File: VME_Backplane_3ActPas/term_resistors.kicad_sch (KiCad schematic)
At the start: 32 parts, among them X2H1 HI_L, X2L1 LO_L, X3H1 HI_R, X3L1 LO_R

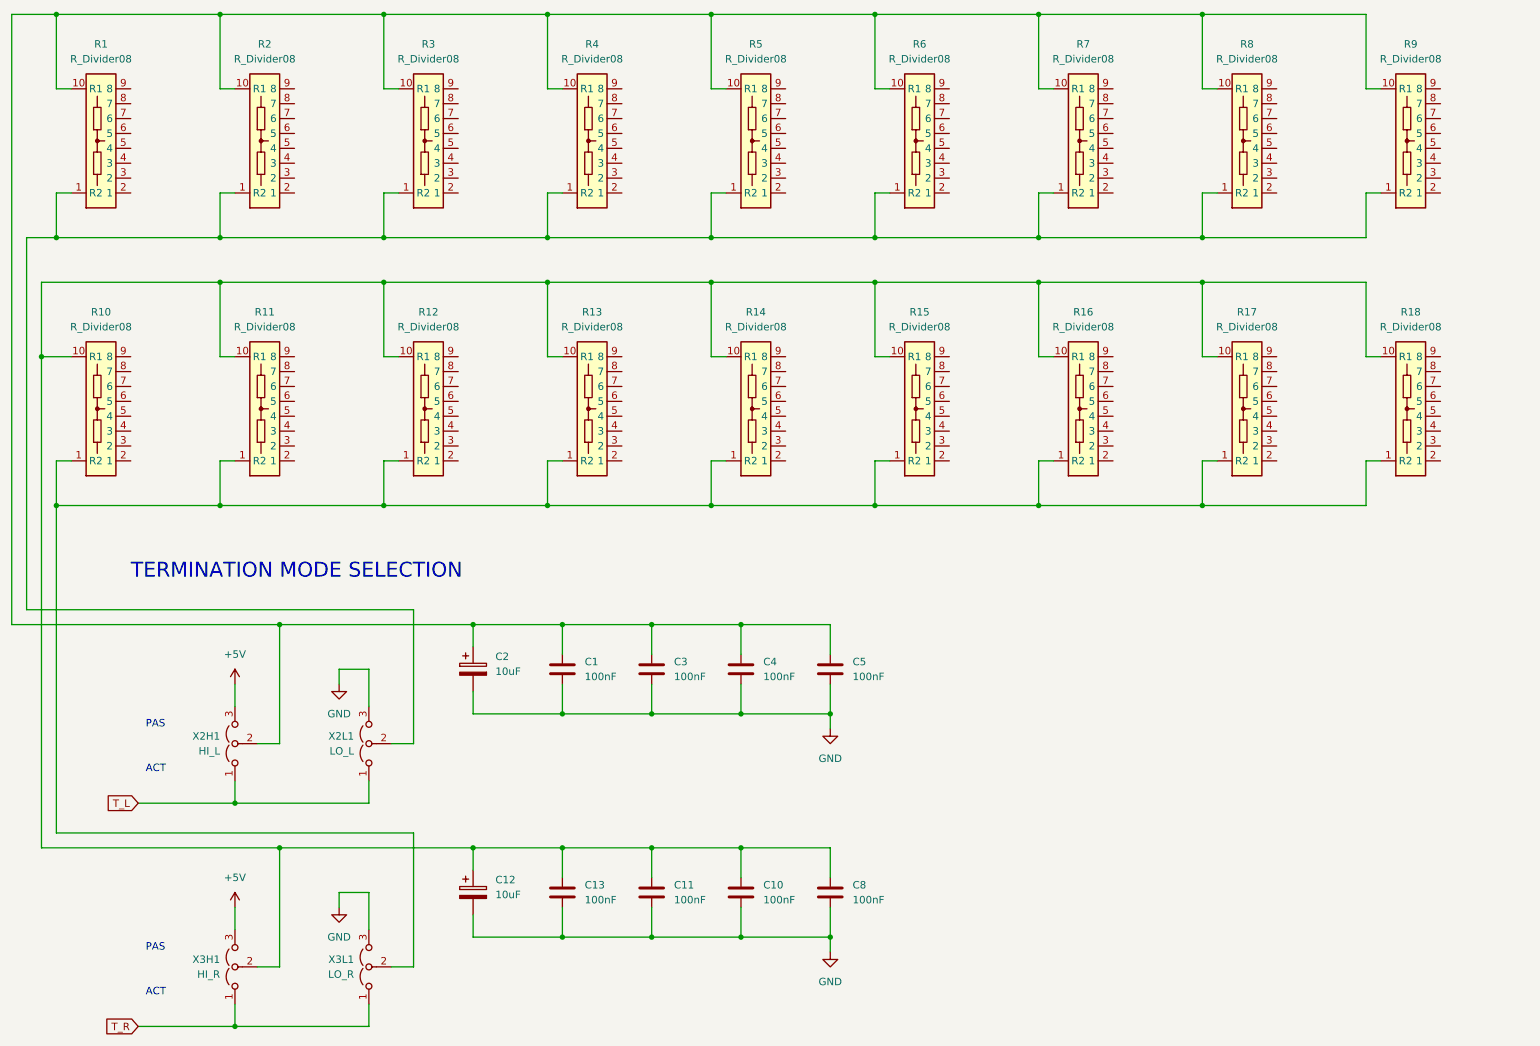
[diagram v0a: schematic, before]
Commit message: Add some kind of filter (?) network for certain critical signals
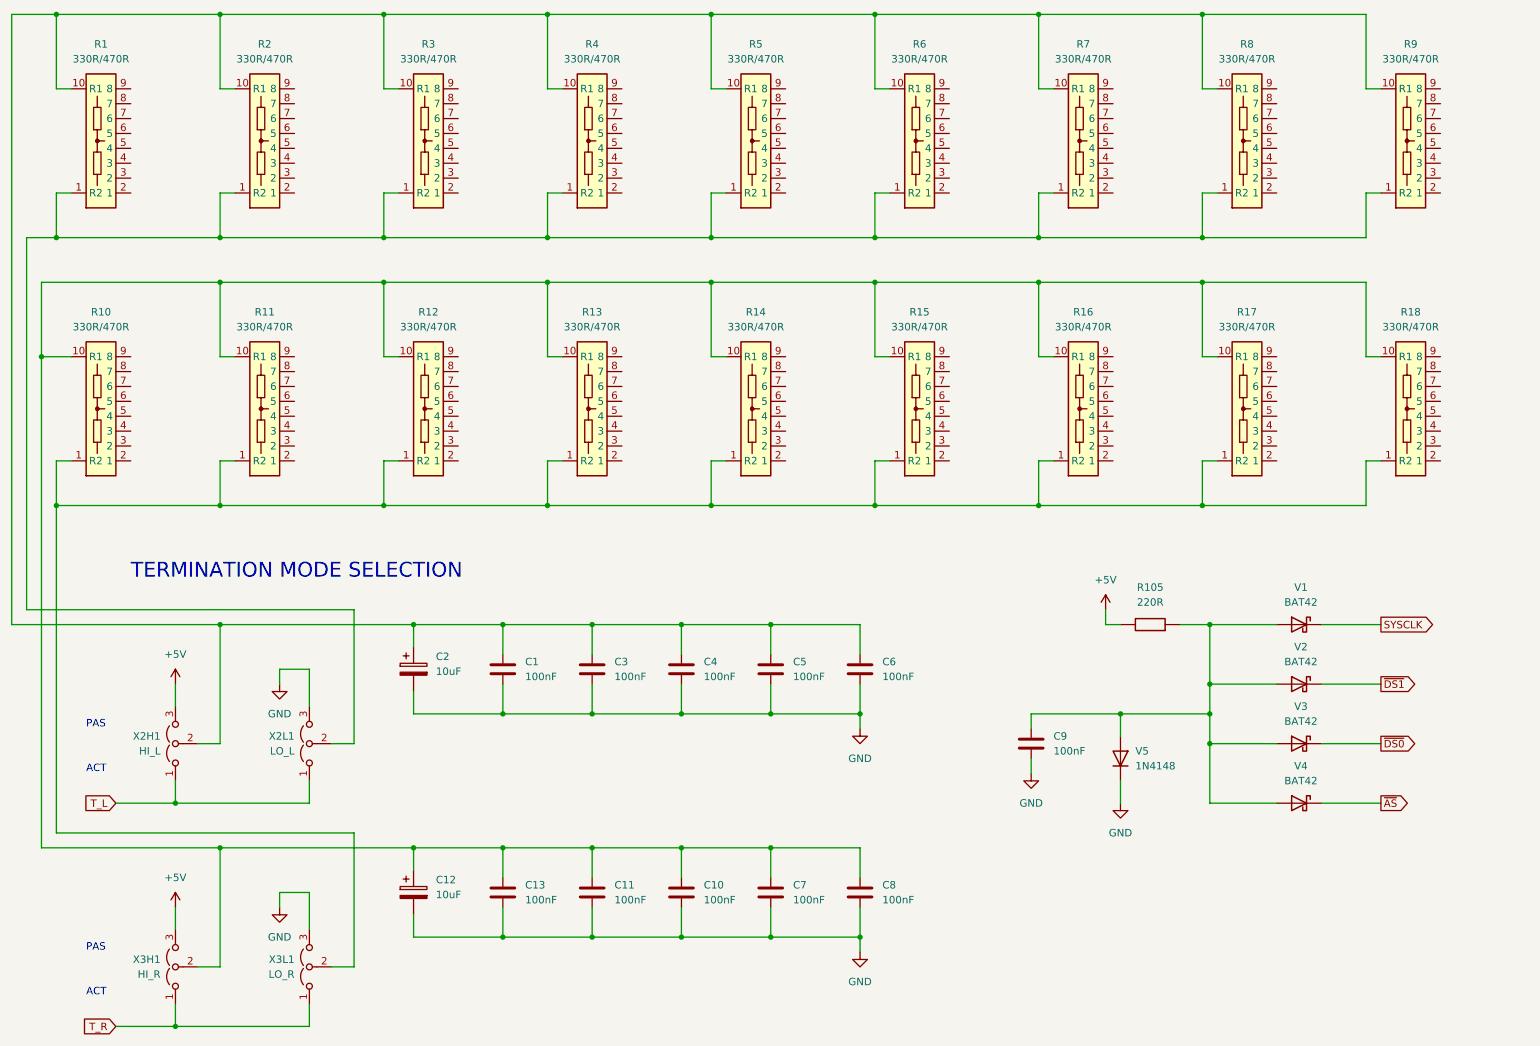
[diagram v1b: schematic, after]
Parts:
- added C6, C7, C9: 100nF, Capacitor_THT:C_Disc_D4.3mm_W1.9mm_P5.00mm, symbol COMET symbols:C
- added R105: 220R, Resistor_THT:R_Axial_DIN0207_L6.3mm_D2.5mm_P10.16mm_Horizontal, symbol COMET symbols:R
- added V1, V2, V3, V4: BAT42, Diode_THT:D_DO-35_SOD27_P10.16mm_Horizontal, symbol Diode:BAT42
- added V5: 1N4148, Diode_THT:D_DO-35_SOD27_P10.16mm_Horizontal, symbol Diode:1N4148
- R1, R10, R11, R12, R13, R14, R15, R16, R17, R18, R2, R3, R4, R5, R6, R7, R8, R9: value R_Divider08 -> 330R/470R
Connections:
- net +5V: now also R105.1
- net GND: now also C6.2, C7.2, C9.2, V5.1 (K)
- net T_L: now also X2H1.1 (A)
- net at C10.1, C11.1, C12.1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: now also C7.1
- net at C1.1, C2.1, C3.1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: now also C6.1
- new net: C9.1, R105.2, V1.2 (A), V2.2 (A), V3.2 (A), V4.2 (A), V5.2 (A)
- new net SYSCLK: V1.1 (K)
- new net ~{AS}: V4.1 (K)
- new net ~{DS0}: V3.1 (K)
- new net ~{DS1}: V2.1 (K)
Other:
- moved on the sheet: C1, C10, C11, C12, C13, C2, C3, C4, C5, C8, X2H1, X2L1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

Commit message: Assign signals to termination resistors
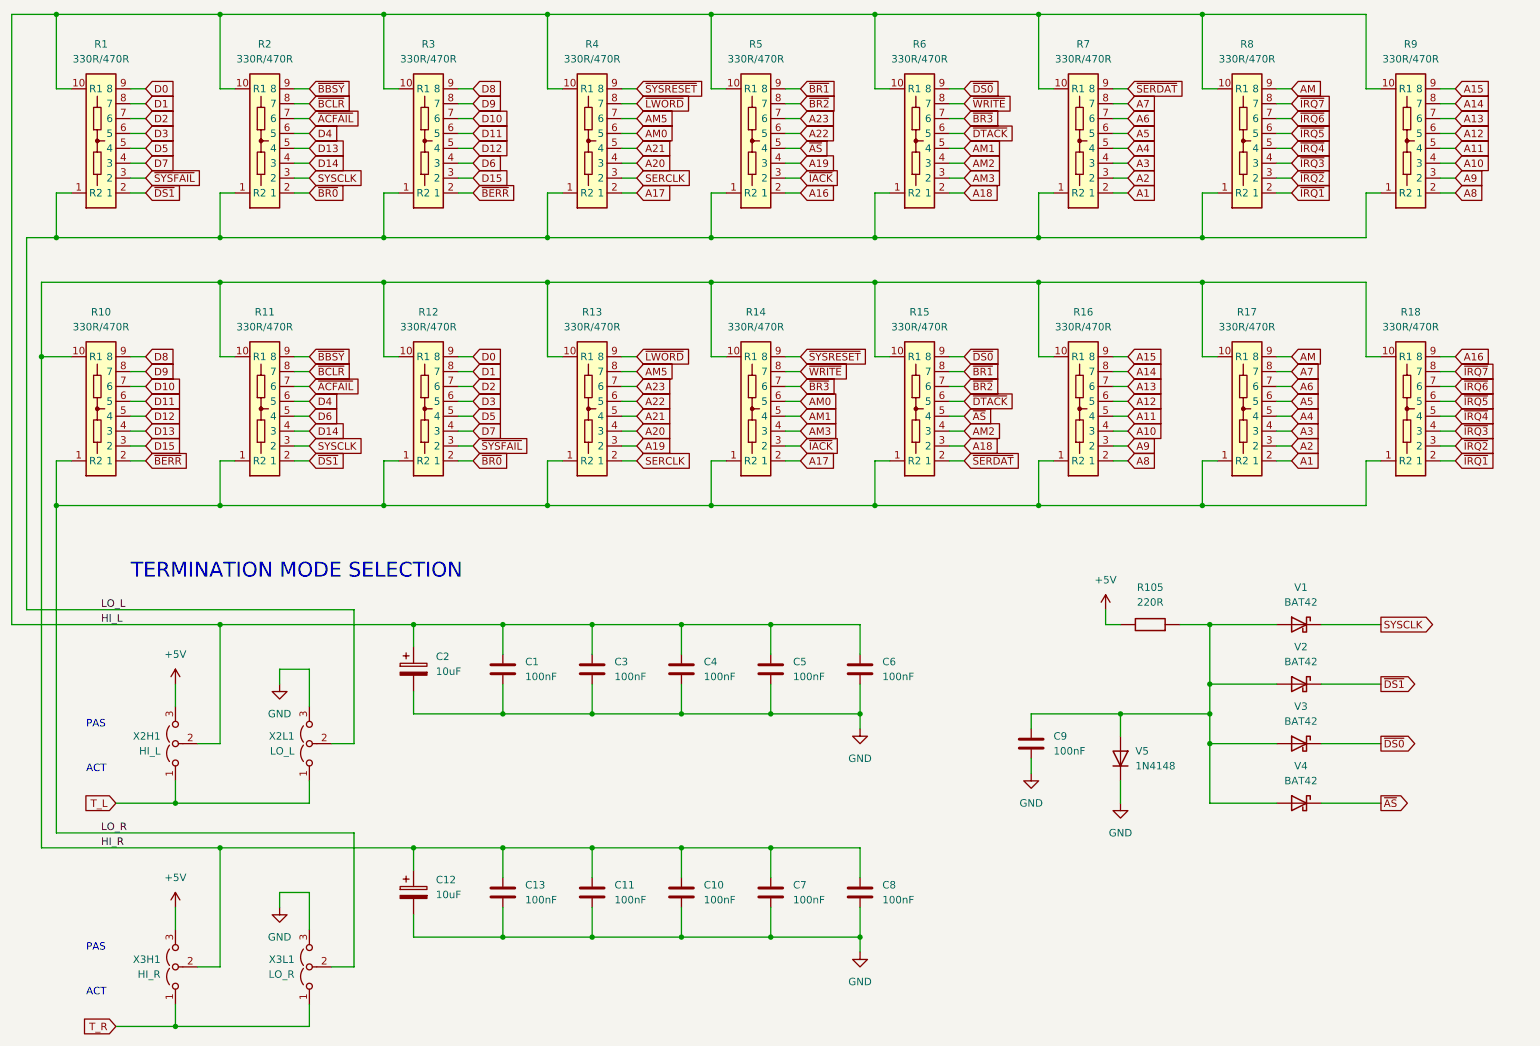
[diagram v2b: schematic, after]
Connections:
- net SYSCLK: now also R11.3 (2), R2.3 (2)
- net ~{AS}: now also R15.5 (4), R5.5 (4)
- net ~{DS0}: now also R15.9 (8), R6.9 (8)
- net ~{DS1}: now also R1.2 (1), R11.2 (1)
- net LO_R: now reaches R10.1 (R2), R11.1 (R2), R12.1 (R2), R13.1 (R2), R14.1 (R2), R15.1 (R2), R16.1 (R2), R17.1 (R2), R18.1 (R2), X3L1.2 (C)
- net HI_R: now reaches C10.1, C11.1, C12.1, C13.1, C7.1, C8.1, R10.10 (R1), R11.10 (R1), R12.10 (R1), R13.10 (R1), R14.10 (R1), R15.10 (R1), R16.10 (R1), R17.10 (R1), R18.10 (R1), X3H1.2 (C)
- net A17: now reaches R14.2 (1)
- net A17: now also R4.2 (1)
- net ~{IACK}: now reaches R14.3 (2)
- net ~{IACK}: now also R5.3 (2)
- net AM3: now reaches R14.4 (3)
- net AM3: now also R6.3 (2)
- net AM1: now reaches R14.5 (4)
- net AM1: now also R6.5 (4)
- net AM0: now reaches R14.6 (5)
- net AM0: now also R4.6 (5)
- net ~{BR3}: now reaches R14.7 (6)
- net ~{BR3}: now also R6.7 (6)
- net ~{WRITE}: now reaches R14.8 (7)
- net ~{WRITE}: now also R6.8 (7)
- net ~{SYSRESET}: now reaches R14.9 (8)
- net ~{SYSRESET}: now also R4.9 (8)
- net ~{IRQ1}: now reaches R18.2 (1)
- net ~{IRQ1}: now also R8.2 (1)
- net ~{IRQ2}: now reaches R18.3 (2)
- net ~{IRQ2}: now also R8.3 (2)
- net ~{IRQ3}: now reaches R18.4 (3)
- net ~{IRQ3}: now also R8.4 (3)
- net ~{IRQ4}: now reaches R18.5 (4)
- net ~{IRQ4}: now also R8.5 (4)
- net ~{IRQ5}: now reaches R18.6 (5)
- net ~{IRQ5}: now also R8.6 (5)
- net ~{IRQ6}: now reaches R18.7 (6)
- net ~{IRQ6}: now also R8.7 (6)
- net ~{IRQ7}: now reaches R18.8 (7)
- net ~{IRQ7}: now also R8.8 (7)
- net A16: now reaches R18.9 (8)
- net A16: now also R5.2 (1)
- net ~{BR0}: now reaches R12.2 (1)
- net ~{BR0}: now also R2.2 (1)
- net ~{SYSFAIL}: now reaches R12.3 (2)
- net ~{SYSFAIL}: now also R1.3 (2)
- net D7: now reaches R12.4 (3)
- net D7: now also R1.4 (3)
- net D5: now reaches R12.5 (4)
- net D5: now also R1.5 (4)
- net D3: now reaches R12.6 (5)
- net D3: now also R1.6 (5)
- net D2: now reaches R12.7 (6)
- net D2: now also R1.7 (6)
- net D1: now reaches R12.8 (7)
- net D1: now also R1.8 (7)
- net D0: now reaches R12.9 (8)
- net D0: now also R1.9 (8)
- net LO_L: now reaches R1.1 (R2), R2.1 (R2), R3.1 (R2), R4.1 (R2), R5.1 (R2), R6.1 (R2), R7.1 (R2), R8.1 (R2), R9.1 (R2), X2L1.2 (C)
- net HI_L: now reaches C1.1, C2.1, C3.1, C4.1, C5.1, C6.1, R1.10 (R1), R2.10 (R1), R3.10 (R1), R4.10 (R1), R5.10 (R1), R6.10 (R1), R7.10 (R1), R8.10 (R1), R9.10 (R1), X2H1.2 (C)
- net ~{BERR}: now reaches R3.2 (1)
- net ~{BERR}: now also R10.2 (1)
- net D15: now reaches R3.3 (2)
- net D15: now also R10.3 (2)
- net D6: now reaches R3.4 (3)
- net D6: now also R11.5 (4)
- net D12: now reaches R3.5 (4)
- net D12: now also R10.5 (4)
- net D11: now reaches R3.6 (5)
- net D11: now also R10.6 (5)
- net D10: now reaches R3.7 (6)
- net D10: now also R10.7 (6)
- net D9: now reaches R3.8 (7)
- net D9: now also R10.8 (7)
- net D8: now reaches R3.9 (8)
- net D8: now also R10.9 (8)
- net A19: now reaches R5.4 (3)
- net A19: now also R13.3 (2)
- net A22: now reaches R5.6 (5)
- net A22: now also R13.6 (5)
- net A23: now reaches R5.7 (6)
- net A23: now also R13.7 (6)
- net ~{BR2}: now reaches R5.8 (7)
- net ~{BR2}: now also R15.7 (6)
- net ~{BR1}: now reaches R5.9 (8)
- net ~{BR1}: now also R15.8 (7)
- net A8: now reaches R16.2 (1)
- net A8: now also R9.2 (1)
- net A9: now reaches R16.3 (2)
- net A9: now also R9.3 (2)
- net A10: now reaches R16.4 (3)
- net A10: now also R9.4 (3)
- net A11: now reaches R16.5 (4)
- net A11: now also R9.5 (4)
- net A12: now reaches R16.6 (5)
- net A12: now also R9.6 (5)
- net A13: now reaches R16.7 (6)
- net A13: now also R9.7 (6)
- net A14: now reaches R16.8 (7)
- net A14: now also R9.8 (7)
- net A15: now reaches R16.9 (8)
- net A15: now also R9.9 (8)
- net SERCLK: now reaches R4.3 (2)
- net SERCLK: now also R13.2 (1)
- net A20: now reaches R4.4 (3)
- net A20: now also R13.4 (3)
- net A21: now reaches R4.5 (4)
- net A21: now also R13.5 (4)
- net AM5: now reaches R4.7 (6)
- net AM5: now also R13.8 (7)
- net ~{LWORD}: now reaches R4.8 (7)
- net ~{LWORD}: now also R13.9 (8)
- net A18: now reaches R6.2 (1)
- net A18: now also R15.3 (2)
- net AM2: now reaches R6.4 (3)
- net AM2: now also R15.4 (3)
- net ~{DTACK}: now reaches R6.6 (5)
- net ~{DTACK}: now also R15.6 (5)
- net ~{SERDAT}: now reaches R15.2 (1)
- net ~{SERDAT}: now also R7.9 (8)
- net A1: now reaches R17.2 (1)
- net A1: now also R7.2 (1)
- net A2: now reaches R17.3 (2)
- net A2: now also R7.3 (2)
- net A3: now reaches R17.4 (3)
- net A3: now also R7.4 (3)
- net A4: now reaches R17.5 (4)
- net A4: now also R7.5 (4)
- net A5: now reaches R17.6 (5)
- net A5: now also R7.6 (5)
- net A6: now reaches R17.7 (6)
- net A6: now also R7.7 (6)
- net A7: now reaches R17.8 (7)
- net A7: now also R7.8 (7)
- net AM: now reaches R17.9 (8)
- net AM: now also R8.9 (8)
- net D13: now reaches R10.4 (3)
- net D13: now also R2.5 (4)
- net D14: now reaches R11.4 (3)
- net D14: now also R2.4 (3)
- net D4: now reaches R11.6 (5)
- net D4: now also R2.6 (5)
- net ~{ACFAIL}: now reaches R11.7 (6)
- net ~{ACFAIL}: now also R2.7 (6)
- net ~{BCLR}: now reaches R11.8 (7)
- net ~{BCLR}: now also R2.8 (7)
- net ~{BBSY}: now reaches R11.9 (8)
- net ~{BBSY}: now also R2.9 (8)

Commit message: Add/update revision information in schematics and PCB
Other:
- company: (C) TOM STOREY -> TOM STOREY
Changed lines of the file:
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@@
   (title_block
     (title "TERMINATION RESISTORS")
-    (date "2024-01-02")
+    (date "2024-01-03")
     (rev "1")
-    (company "(C) TOM STOREY")
+    (company "TOM STOREY")
     (comment 1 "FREE FOR NON-COMMERCIAL USE")
   )
